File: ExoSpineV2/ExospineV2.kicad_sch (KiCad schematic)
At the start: 59 parts, among them J1 GPIO, J15 Conn_01x02, J16 Conn_01x02, J17 Conn_01x02, J19 Conn_01x03, J20 Conn_01x03, J21 Conn_01x03, J22 Conn_01x02, J23 Conn_01x02, J24 Conn_01x02, J25 Conn_01x03, J26 Conn_01x03, J27 Conn_01x04, J28 Conn_01x03, J29 Conn_01x03, J30 Conn_01x02, J31 Conn_01x03, J32 Conn_01x03, J33 Conn_01x03, J34 Conn_01x03, Q10 Q_NMOS_DGS, Q11 Q_NMOS_DGS, Q6 Q_NMOS_DGS, Q7 Q_NMOS_DGS, Q8 Q_NMOS_DGS, Q9 Q_NMOS_DGS, U4 74HC00, U5 74HC00, U6 MCP3008

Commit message: Modified temperature sensors connectors
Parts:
- removed C12, C13, C14, C15: 1u, symbol Device:C_Small
- removed J28, J31, J32, J33: Conn_01x03, symbol Connector_Generic:Conn_01x03
- removed R19, R20, R21, R25: 4.7k, Resistor_SMD:R_0402_1005Metric, symbol Device:R
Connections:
- net +12V: now reaches J20.1 (Pin_1)
- net +12V: now also J19.1 (Pin_1), J21.1 (Pin_1)
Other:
- note removed: "Temperature Sensor 1"
- note removed: "Temperature Sensor 2"
- note removed: "Temperature Sensor 3"
- note removed: "Temperature Sensor 4"
- note removed: "Temperature Sensor 5"
- moved on the sheet: C26, J16, J17, J20, J21, J23, J25, J29, J30, J34, Q10, Q11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

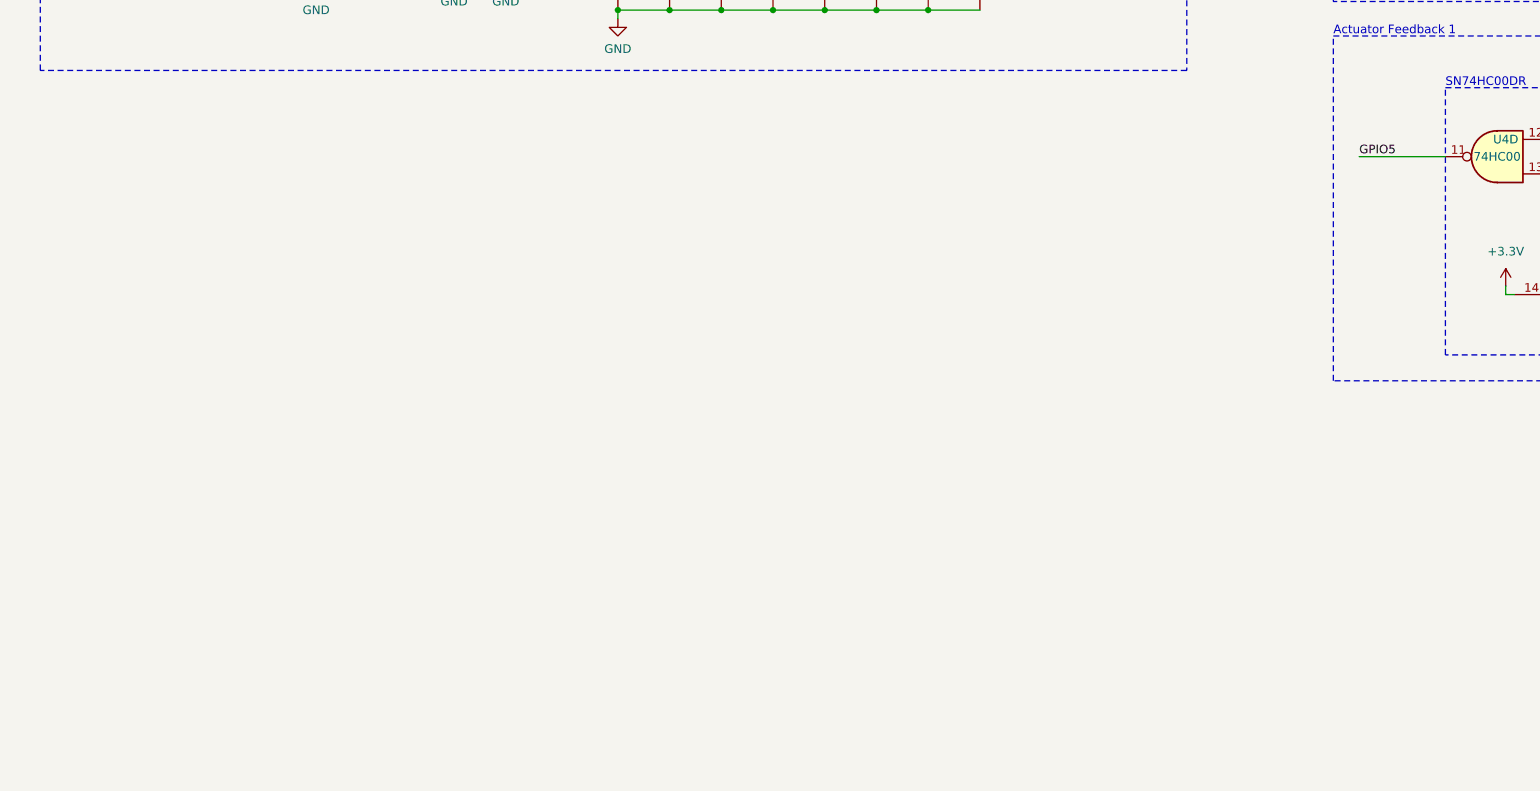
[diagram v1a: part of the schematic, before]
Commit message: planned mux and LTC2942
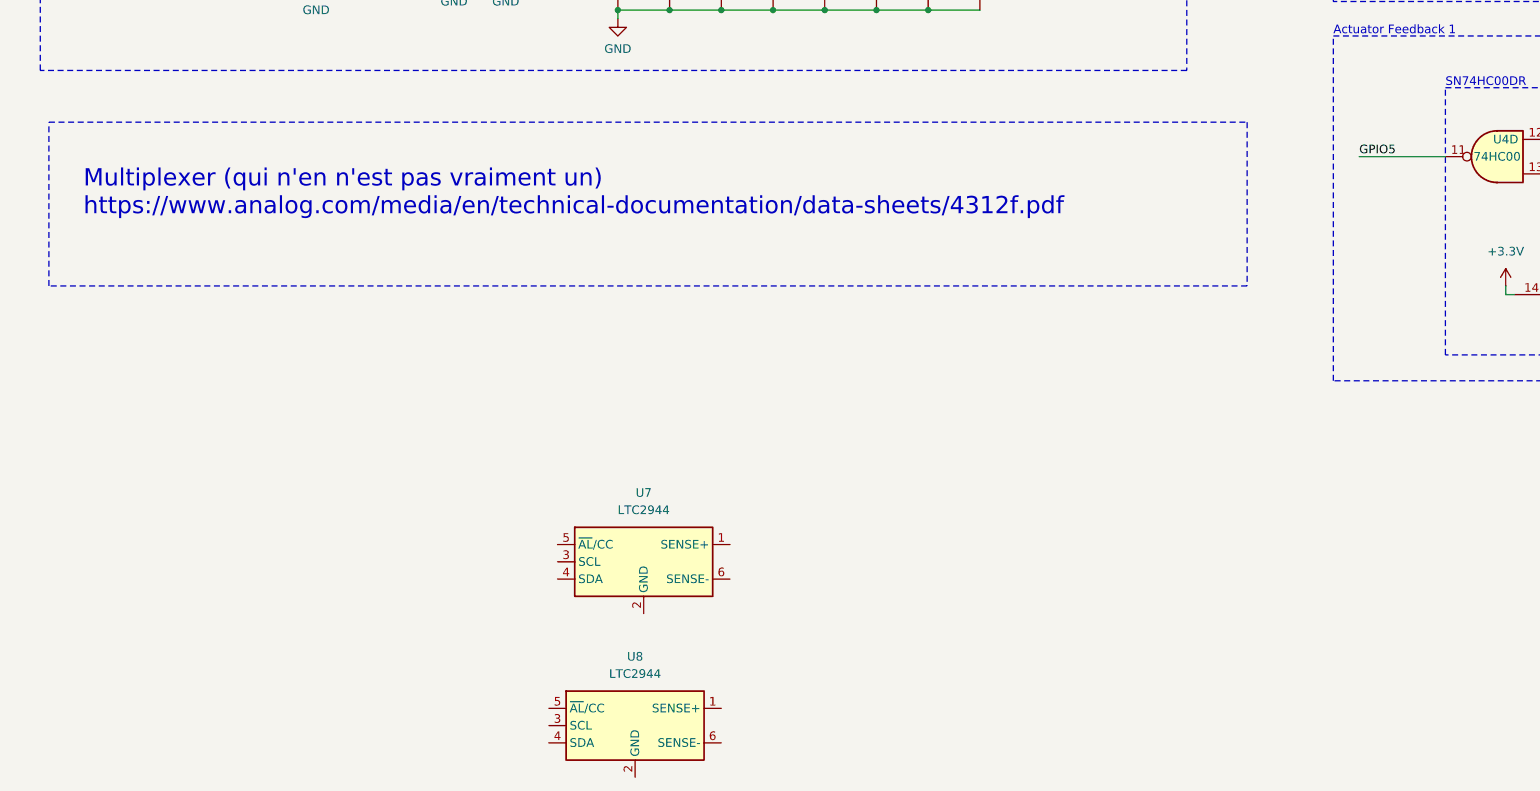
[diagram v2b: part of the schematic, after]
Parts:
- added U7, U8: LTC2944, Package_DFN_QFN:DFN-6-1EP_3x2mm_P0.5mm_EP1.65x1.35mm, symbol Battery_Management:LTC2942
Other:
- note added: "Multiplexer (qui n'en n'est pas vraiment un) https://www.analog.com/media/en/technical-documentation/data-sheets/4312f.pdf"
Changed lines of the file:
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@@
+    (fill (type none))
+  )
+  (rectangle (start 20.32 190.5) (end 196.85 214.63)
+    (stroke (width 0) (type dash) (color 0 194 0 1))
     (fill (type none))
   )
@@
   (text "Analog to Digital Converter (ADC) - MCP3008\n" (at 19.05 124.46 0)
     (effects (font (size 1.27 1.27) (color 0 194 0 1)) (justify left bottom))
+  )
+  (text "Multiplexer (qui n'en n'est pas vraiment un)\nhttps://www.analog.com/media/en/technical-documentation/data-sheets/4312f.pdf"
+    (at 25.4 204.47 0)
+    (effects (font (size 2.54 2.54)) (justify left bottom))
   )
   (text "SN74HC00DR" (at 226.06 185.42 0)
@@
     )
   )
+  (symbol (lib_id "Battery_Management:LTC2942") (at 107.95 255.27 0) (unit 1)
+    (in_bom yes) (on_board yes) (dnp no) (fields_autoplaced)
+    (property "Reference" "U7" (at 107.95 245.11 0)
+      (effects (font (size 1.27 1.27)))
+    )
+    (property "Value" "LTC2944" (at 107.95 247.65 0)
+      (effects (font (size 1.27 1.27)))
+    )
+    (property "Footprint" "Package_DFN_QFN:DFN-6-1EP_3x2mm_P0.5mm_EP1.65x1.35mm" (at 107.95 246.38 0)
+      (effects (font (size 1.27 1.27)) hide)
+    )
+    (property "Datasheet" "https://www.analog.com/media/en/technical-documentation/data-sheets/2944fa.pdf" (at 107.95 256.54 0)
+      (effects (font (size 1.27 1.27)) hide)
+    )
+    (pin "1")
+    (pin "2")
+    (pin "6")
+    (pin "5")
+    (pin "4")
+    (pin "3")
+    (instances
+      (project "ExospineV2"
+        (path "/e63e39d7-6ac0-4ffd-8aa3-1841a4541b55"
+          (reference "U7") (unit 1)
+        )
+      )
+    )
+  )
   (symbol (lib_id "Device:Q_NMOS_DGS") (at 238.76 116.84 0) (unit 1)
     (in_bom yes) (on_board yes) (dnp no) (fields_autoplaced)
@@
         )
       )
+    )
+  )
+  (symbol (lib_id "Battery_Management:LTC2942") (at 106.68 279.4 0) (unit 1)
+    (in_bom yes) (on_board yes) (dnp no) (fields_autoplaced)
+    (property "Reference" "U8" (at 106.68 269.24 0)
+      (effects (font (size 1.27 1.27)))
+    )
+    (property "Value" "LTC2944" (at 106.68 271.78 0)
+      (effects (font (size 1.27 1.27)))
+    )
+    (property "Footprint" "Package_DFN_QFN:DFN-6-1EP_3x2mm_P0.5mm_EP1.65x1.35mm" (at 106.68 270.51 0)
+      (effects (font (size 1.27 1.27)) hide)
+    )
+    (property "Datasheet" "https://www.analog.com/media/en/technical-documentation/data-sheets/2944fa.pdf" (at 106.68 280.67 0)
+      (effects (font (size 1.27 1.27)) hide)
+    )
+    (pin "1")
+    (pin "2")
+    (pin "6")
+    (pin "5")
+    (pin "4")
+    (pin "3")
+    (instances
+      (project "ExospineV2"
+        (path "/e63e39d7-6ac0-4ffd-8aa3-1841a4541b55"
+          (reference "U8") (unit 1)
+        )
+      )

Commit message: added LTC4312 circuit
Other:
- added sheet LTC4312 (LTC4312.kicad_sch)
- note added: "LTC4312 (I2C Multiplexer)"
- note removed: "12V or 5V ????"
- note removed: "Multiplexer (qui n'en n'est pas vraiment un) https://www.analog.com/media/en/technical-documentation/data-sheets/4312f.pdf"
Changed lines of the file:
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@@
     (fill (type none))
   )
+  (rectangle (start 481.965 291.465) (end 517.525 300.355)
+    (stroke (width 0) (type default) (color 194 0 194 1))
+    (fill (type none))
+  )
   (rectangle (start 316.23 185.42) (end 361.95 224.79)
     (stroke (width 0) (type dash) (color 0 194 0 1))
@@
     (fill (type none))
   )
-  (rectangle (start 20.32 190.5) (end 196.85 214.63)
+  (rectangle (start 481.33 290.83) (end 518.16 300.99)
+    (stroke (width 0) (type default) (color 194 0 194 1))
+    (fill (type none))
+  )
+  (rectangle (start 19.05 193.04) (end 50.8 214.63)
     (stroke (width 0) (type dash) (color 0 194 0 1))
     (fill (type none))
@@
     (fill (type none))
   )
+  (rectangle (start 20.32 95.25) (end 64.77 114.3)
+    (stroke (width 0) (type default) (color 194 0 0 1))
+    (fill (type none))
+  )
   (rectangle (start 209.55 142.24) (end 266.7 172.72)
     (stroke (width 0) (type dash))
@@
     (fill (type none))
   )
-  (rectangle (start 19.05 93.98) (end 63.5 115.57)
+  (rectangle (start 19.05 93.98) (end 66.04 115.57)
     (stroke (width 0) (type default) (color 194 0 0 1))
     (fill (type none))
@@
     (effects (font (size 1.27 1.27)) (justify left bottom))
   )
-  (text "Itération précédente du \nschéma du PCB et layout électrique\n"
-    (at 483.87 269.24 0)
-    (effects (font (size 1.27 1.27)) (justify left bottom))
+  (text "Itération précédente du schéma\ndu PCB et layout électrique\n"
+    (at 481.33 290.83 0)
+    (effects (font (size 1.27 1.27) (color 194 0 194 1)) (justify left bottom))
   )
   (text "Contactor Control 2" (at 266.7 57.15 0)
@@
     (effects (font (size 1.27 1.27) (color 0 194 0 1)) (justify left bottom))
   )
-  (text "Multiplexer (qui n'en n'est pas vraiment un)\nhttps://www.analog.com/media/en/technical-documentation/data-sheets/4312f.pdf"
-    (at 25.4 204.47 0)
-    (effects (font (size 2.54 2.54)) (justify left bottom))
+  (text "LTC4312 (I2C Multiplexer)" (at 19.05 193.04 0)
+    (effects (font (size 1.27 1.27) (color 0 194 0 1)) (justify left bottom))
   )
   (text "SN74HC00DR" (at 226.06 185.42 0)
@@
     (effects (font (size 1.27 1.27) (color 132 132 132 1)) (justify left bottom))
   )
-  (text "12V or 5V ????" (at 222.25 64.77 0)
-    (effects (font (size 2.54 2.54) (thickness 0.508) bold (color 255 0 0 1)) (justify left bottom))
-  )
   (text "SN74HC00DR" (at 316.23 185.42 0)
     (effects (font (size 1.27 1.27) (color 0 194 0 1)) (justify left bottom))
@@
     )
   )
-  (sheet (at 490.22 273.05) (size 26.67 7.62) (fields_autoplaced)
+  (sheet (at 22.86 198.12) (size 22.86 10.16) (fields_autoplaced)
+    (stroke (width 0.1524) (type solid))
+    (fill (color 255 229 191 1.0000))
+    (property "Sheetname" "LTC4312" (at 22.86 197.4084 0)
+      (effects (font (size 1.27 1.27)) (justify left bottom))
+    )
+    (property "Sheetfile" "LTC4312.kicad_sch" (at 22.86 208.8646 0)
+      (effects (font (size 1.27 1.27)) (justify left top))
+    )
+    (instances
+      (project "ExospineV2"
+        (path "/e63e39d7-6ac0-4ffd-8aa3-1841a4541b55" (page "4"))
+      )
+    )
+  )
+  (sheet (at 484.505 294.005) (size 26.67 3.81) (fields_autoplaced)
     (stroke (width 0.1524) (type solid))
-    (fill (color 0 0 0 0.0000))
-    (property "Sheetname" "ExoSpineV1" (at 490.22 272.3384 0)
+    (fill (color 255 229 191 1.0000))
+    (property "Sheetname" "ExoSpineV1" (at 484.505 293.2934 0)
       (effects (font (size 1.27 1.27)) (justify left bottom))
     )
-    (property "Sheetfile" "ExoSpineV1.kicad_sch" (at 490.22 281.2546 0)
+    (property "Sheetfile" "ExoSpineV1.kicad_sch" (at 484.505 298.3996 0)
       (effects (font (size 1.27 1.27)) (justify left top))
     )
@@
     )
   )
-  (sheet (at 29.21 100.33) (size 26.67 11.43) (fields_autoplaced)
+  (sheet (at 22.86 100.33) (size 35.56 8.89) (fields_autoplaced)
     (stroke (width 0.1524) (type solid))
-    (fill (color 0 0 0 0.0000))
-    (property "Sheetname" "12v-5v buck converter" (at 29.21 99.6184 0)
+    (fill (color 255 229 191 1.0000))
+    (property "Sheetname" "12v-5v buck converter" (at 22.86 99.6184 0)
       (effects (font (size 1.27 1.27)) (justify left bottom))
     )
-    (property "Sheetfile" "12v-5vBuckConverter.kicad_sch" (at 29.21 112.3446 0)
+    (property "Sheetfile" "12v-5vBuckConverter.kicad_sch" (at 22.86 109.8046 0)
       (effects (font (size 1.27 1.27)) (justify left top))
     )

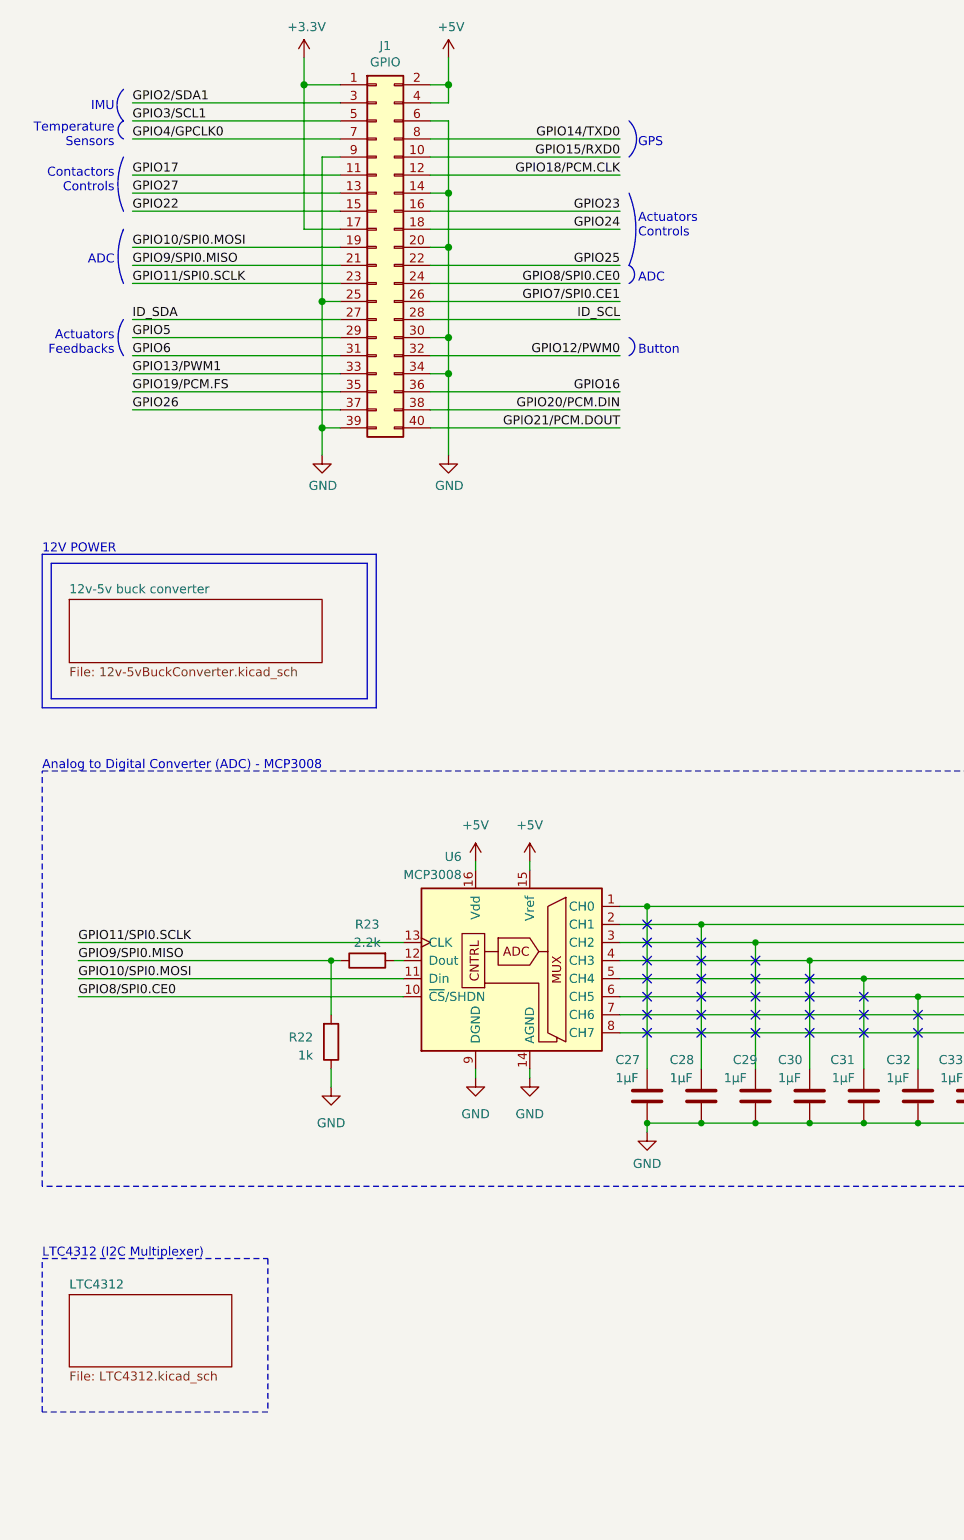
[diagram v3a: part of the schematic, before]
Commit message: Added connections to batteries PCBs
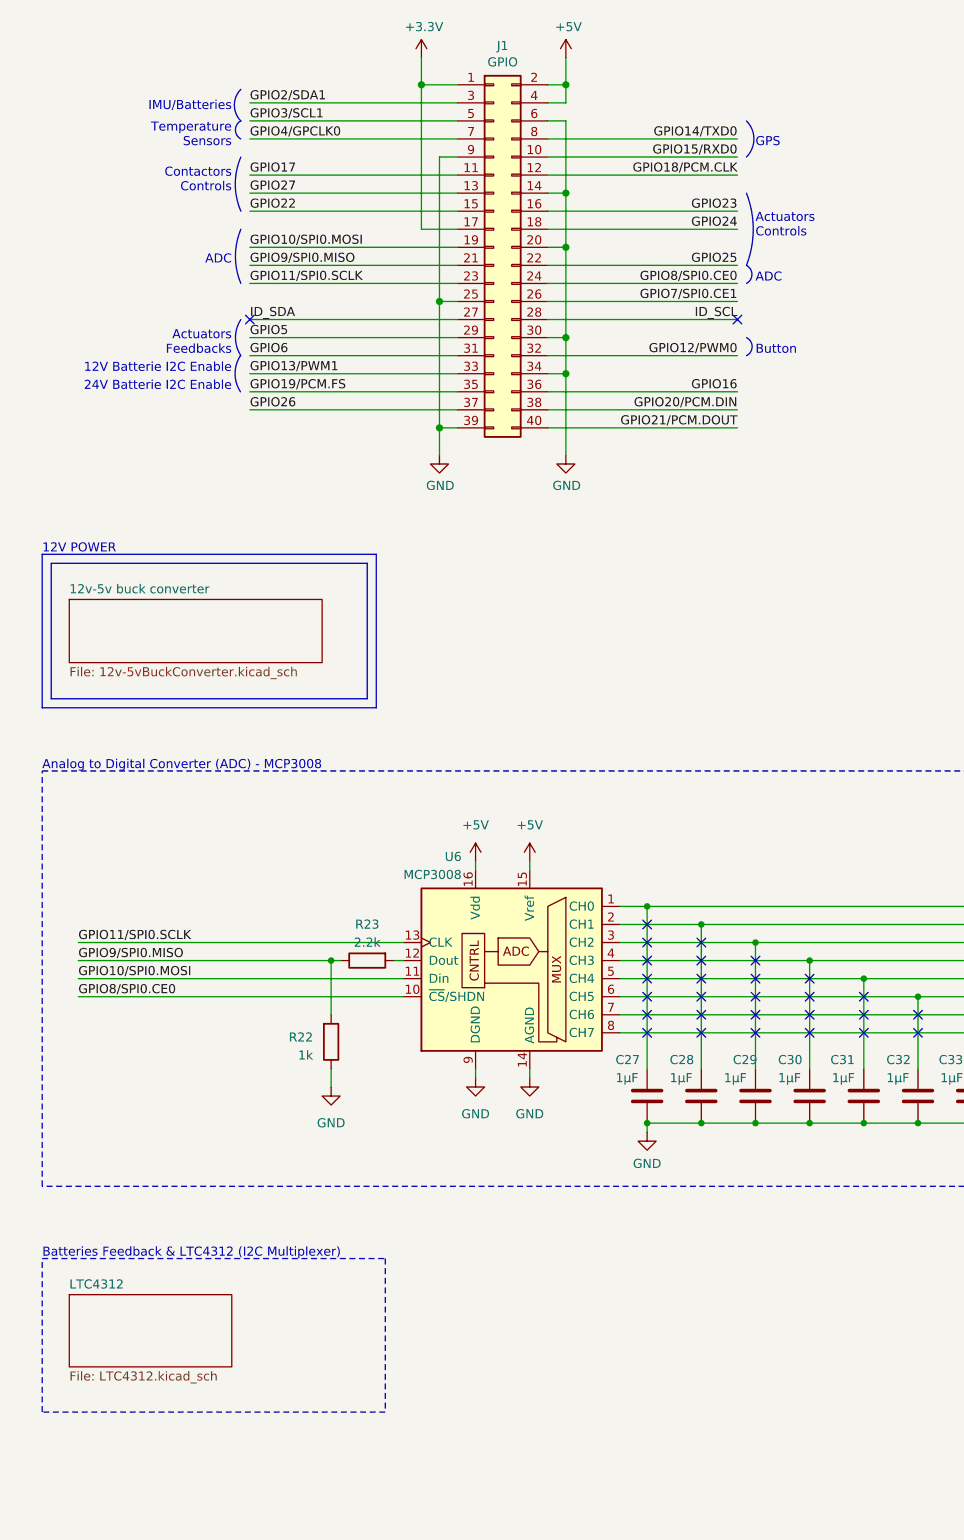
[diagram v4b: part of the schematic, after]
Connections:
- no-connect marks 28 -> 30
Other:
- note added: "12V Batterie I2C Enable"
- note added: "24V Batterie I2C Enable"
- note added: "Batteries Feedback & LTC4312 (I2C Multiplexer)"
- note added: "IMU/Batteries"
- note removed: "LTC4312 (I2C Multiplexer)"
- moved on the sheet: J1

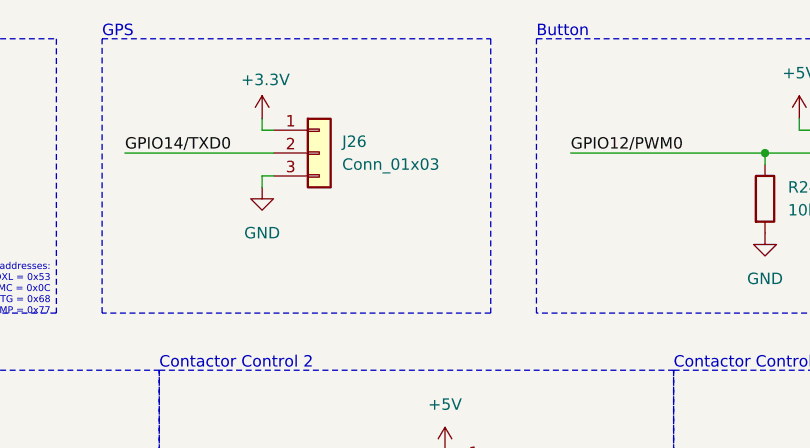
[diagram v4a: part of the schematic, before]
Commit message: added connection type for GPS
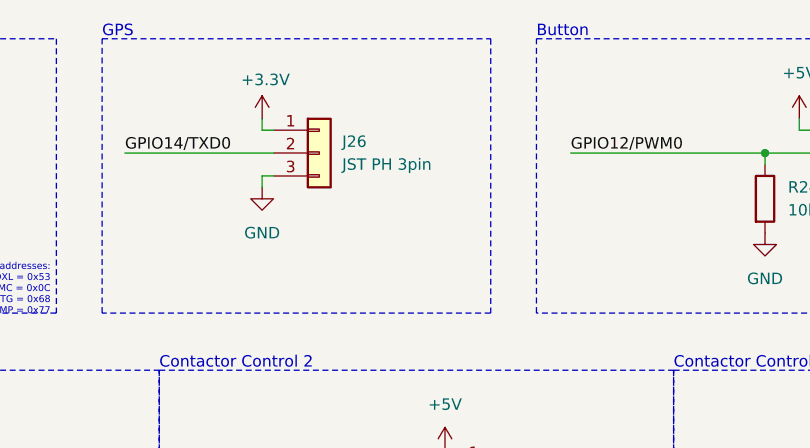
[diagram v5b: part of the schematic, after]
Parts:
- J26: value Conn_01x03 -> JST PH 3pin; footprint (none) -> Connector_JST:JST_PH_B2B-PH-K_1x02_P2.00mm_Vertical
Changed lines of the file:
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@@
       (effects (font (size 1.27 1.27)) (justify left))
     )
-    (property "Value" "Conn_01x03" (at 287.02 34.29 0)
+    (property "Value" "JST PH 3pin" (at 287.02 34.29 0)
       (effects (font (size 1.27 1.27)) (justify left))
     )
-    (property "Footprint" "" (at 284.48 33.02 0)
+    (property "Footprint" "Connector_JST:JST_PH_B2B-PH-K_1x02_P2.00mm_Vertical" (at 284.48 33.02 0)
       (effects (font (size 1.27 1.27)) hide)
     )
